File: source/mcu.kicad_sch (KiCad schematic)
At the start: 35 parts, among them J4 Conn_01x04_Male, J5 TYPE-C-31-M-12, U14 TJA1050T/CM,118, U15 STM32F405RGT6, Y1 8MHz Crystal Resonator, X5032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

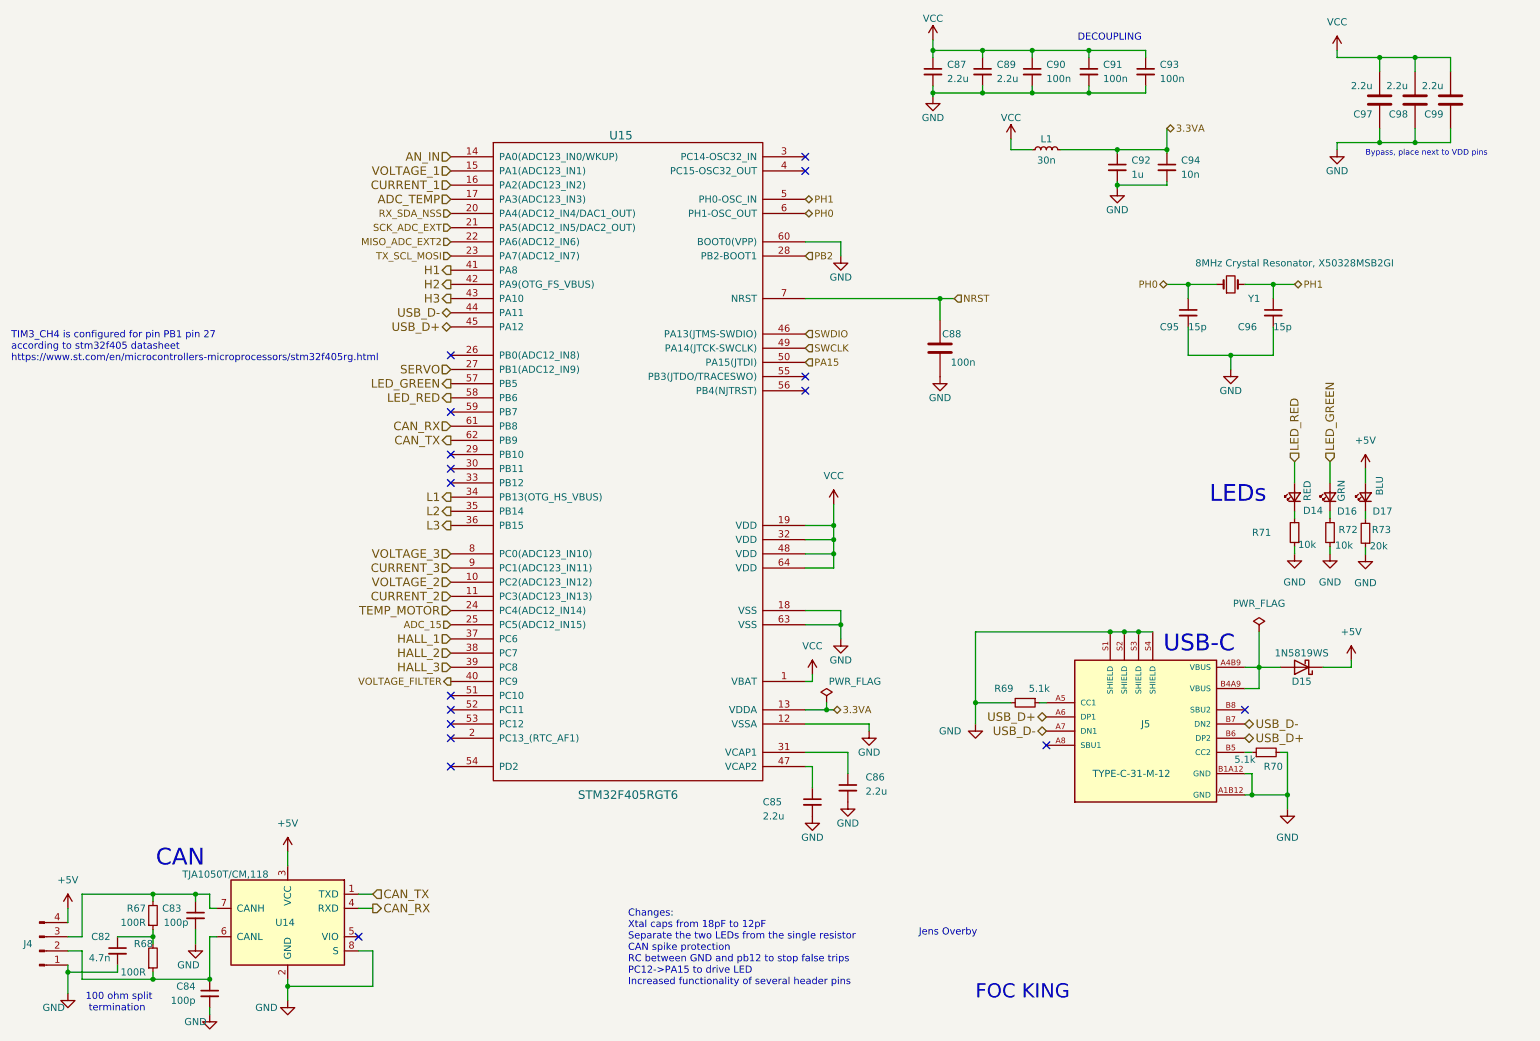
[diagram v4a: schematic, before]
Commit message: Add files via upload
Filter resistor on current op-amps changed from 30k to 150R
Mosfets at 45 deg angle
Changed layout of power supply
Cut through center of board
Unnecessary components near mosfets removed
Voltage filters removed again
Crystal suspected noise source - moved to back of board
Current sensing moved to in0 - in2 (PA0-PA2)
Voltage sensing moved to in11-in13
Supply voltage moved to in10
Mosfets can now be attached to heat-sink plate using screws (that can be tightened throug holes in the board)
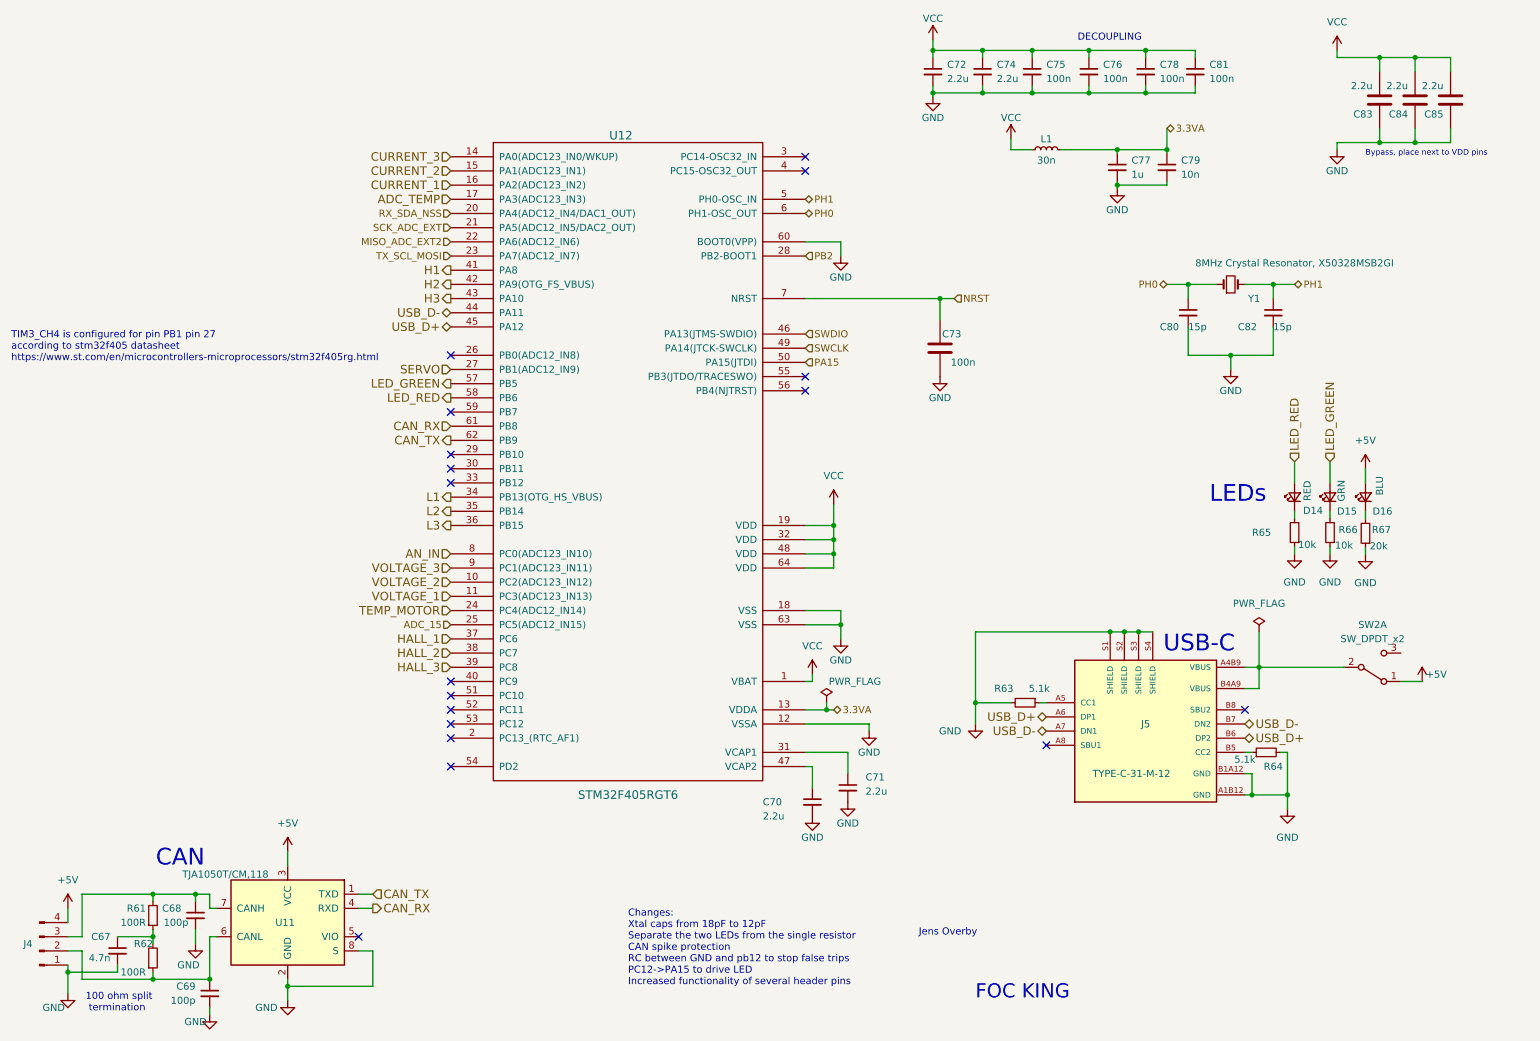
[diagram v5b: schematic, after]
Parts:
- removed D15: 1N5819WS, Diode_SMD:D_SOD-323, symbol Device:D_Schottky
- added C81: 100n, Capacitor_SMD:C_0603_1608Metric, symbol Device:C_Small
- added SW2: SW_DPDT_x2, Jumper:SolderJumper-2_P1.3mm_Open_Pad1.0x1.5mm, symbol Switch:SW_DPDT_x2
- renumbered C82 to C67, C83 to C68, C84 to C69, C85 to C70, C86 to C71, C87 to C72, C88 to C73, C89 to C74, C90 to C75, C91 to C76, C92 to C77, C93 to C78, C94 to C79, C95 to C80, C96 to C82, C97 to C83, C98 to C84, C99 to C85, D16 to D15, D17 to D16, R67 to R61, R68 to R62, R69 to R63, R70 to R64, R71 to R65, R72 to R66, R73 to R67, U14 to U11, U15 to U12
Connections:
- net +5V: now also SW2.1 (A)
- net AN_IN: now also U12.8 (PC0(ADC123_IN10)); no longer U12.14 (PA0(ADC123_IN0/WKUP))
- net CURRENT_2: now also U12.15 (PA1(ADC123_IN1)); no longer U12.11 (PC3(ADC123_IN13))
- net CURRENT_3: now also U12.14 (PA0(ADC123_IN0/WKUP)); no longer U12.9 (PC1(ADC123_IN11))
- net GND: now also C81.2
- net VCC: now also C81.1
- net VOLTAGE_1: now also U12.11 (PC3(ADC123_IN13)); no longer U12.15 (PA1(ADC123_IN1))
- net VOLTAGE_3: now also U12.9 (PC1(ADC123_IN11)); no longer U12.8 (PC0(ADC123_IN10))
- net at J5.A4B9 (VBUS), J5.B4A9 (VBUS): now also SW2.2 (B)
- net VOLTAGE_FILTER: no longer names the net of U12.40 (PC9)
- no-connect marks 17 -> 18

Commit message: 2 board setup with mcu and foc shield separated
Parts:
- removed C67: 4.7n, Capacitor_SMD:C_0603_1608Metric, symbol Device:C_Small
- removed C68, C69: 100p, Capacitor_SMD:C_0603_1608Metric, symbol Device:C_Small
- removed C72, C74: 2.2u, Capacitor_SMD:C_0603_1608Metric, symbol Device:C_Small
- removed C73: 100n, Capacitor_SMD:C_0603_1608Metric, symbol BLDC_4-rescue:C-RESCUE-BLDC_4
- removed C84, C85: 2.2u, Capacitor_SMD:C_0603_1608Metric, symbol BLDC_4-rescue:C-RESCUE-BLDC_4
- removed J4: Conn_01x04_Male, Connector_PinHeader_2.54mm:PinHeader_1x04_P2.54mm_Vertical, symbol Connector:Conn_01x04_Male
- removed R61, R62: 100R, Resistor_SMD:R_0603_1608Metric, symbol Device:R_Small
- removed U11: TJA1050T/CM,118, Package_SO:SOIC-8_3.9x4.9mm_P1.27mm, symbol Interface_CAN_LIN:TJA1051T-3
- added C67, C68: 100n, Capacitor_SMD:C_0603_1608Metric, symbol Device:C
- added C80: 10u, Capacitor_SMD:C_0603_1608Metric, symbol Device:C
- added JP1: SolderJumper_3_Open, Jumper:SolderJumper-3_P1.3mm_Open_RoundedPad1.0x1.5mm_NumberLabels, symbol Jumper:SolderJumper_3_Open
- added P1: SWD, Connector_PinHeader_2.54mm:PinHeader_1x05_P2.54mm_Vertical, symbol Connector_Generic:Conn_01x05
- added U11, U12: STM32F401CCU6_Blackpill, Custom:Blackpill_STM32F401CEU6, symbol CCC_ESC_Custom_Symbols:STM32F401CCU6_Balckpill
- C76: renamed from C80; value 15p -> 12p; LCSC C1644 -> C38523
- C78: renamed from C82; value 15p -> 12p; LCSC C1644 -> C38523
- C79: renamed from C83; value 2.2u -> 100n; LCSC C23630 -> C14663
- SW2: symbol Switch:SW_DPDT_x2 -> Switch:SW_DPST_x2
- renumbered C70 to C69, C71 to C70, C75 to C71, C76 to C72, C77 to C73, C78 to C74, C79 to C75, C81 to C77, R63 to R60, R64 to R61, R65 to R62, R66 to R63, R67 to R64, U12 to U13
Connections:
- net +5V: now also SW2.2 (B), U11.38 (5V), U12.21 (PB12), U12.38 (5V); no longer SW2.1 (A)
- net ADC_TEMP: now also C68.1, JP1.2 (C), JP1.3 (B), U11.15 (PB1), U12.15 (PB1)
- net AN_IN: now also U11.7 (PA1), U12.7 (PA1)
- net CAN_RX: now also U11.36 (PB8), U12.36 (PB8)
- net CAN_TX: now also U11.37 (PB9), U12.37 (PB9)
- net CURRENT_1: now also U11.8 (PA2), U12.8 (PA2)
- net CURRENT_2: now also U11.9 (PA3), U12.9 (PA3)
- net CURRENT_3: now also U11.10 (PA4), U12.10 (PA4)
- net GND: now also C67.2, C68.2, C80.2, P1.3 (Pin_3), U11.19 (GND), U11.39 (GND), U12.19 (GND), U12.39 (GND)
- net H1: now also U11.25 (PA8), U12.25 (PA8)
- net H2: now also U11.26 (PA9), U12.26 (PA9)
- net H3: now also U11.27 (PA10), U12.27 (PA10)
- net HALL_1: now also U11.2 (PC13), U12.2 (PC13)
- net HALL_2: now also U11.3 (PC14), U12.3 (PC14)
- net HALL_3: now also U11.4 (PC15), U12.4 (PC15)
- net L1: now also U11.22 (PB13), U12.22 (PB13)
- net L2: now also U11.23 (PB14), U12.23 (PB14)
- net L3: now also U11.24 (PB15), U12.24 (PB15)
- net NRST: now also C67.1, JP1.1 (A), P1.5 (Pin_5), U11.5 (NRST), U12.5 (NRST)
- net VCC: now also C80.1, P1.1 (Pin_1), U11.18 (3V3), U11.40 (3V3), U12.18 (3V3), U12.40 (3V3)
- net VOLTAGE_1: now also U11.11 (PA5), U12.11 (PA5)
- net VOLTAGE_2: now also U11.12 (PA6), U12.12 (PA6)
- net VOLTAGE_3: now also U11.14 (PB0), U12.14 (PB0)
- net CONN_12: now reaches U13.55 (PB3(JTDO/TRACESWO))
- net CONN_12: now also U11.6 (PA0), U12.6 (PA0)
- net at J5.A4B9 (VBUS), J5.B4A9 (VBUS): now also SW2.1 (A); no longer SW2.2 (B)
- net ADC_15 renamed CONN_5
- net CONN_5: now also U11.31 (PB3), U12.31 (PB3)
- net MISO_ADC_EXT2 renamed CONN_10
- net CONN_10: now also U11.17 (PB10), U12.17 (PB10)
- net PA15 renamed CONN_7
- net CONN_7: now also U11.33 (PB5), U12.33 (PB5)
- net PB2 renamed CONN_6
- net CONN_6: now also U11.32 (PB4), U12.32 (PB4)
- net RX_SDA_NSS renamed CONN_8
- net CONN_8: now also U11.34 (PB6), U12.34 (PB6)
- net SCK_ADC_EXT renamed CONN_9
- net CONN_9: now also U11.35 (PB7), U12.35 (PB7)
- net SERVO renamed SERVO_MOTORTEMP
- net SERVO_MOTORTEMP: now also U11.13 (PA7), U12.13 (PA7)
- net SWCLK: no longer names the net of U13.49 (PA14(JTCK-SWCLK))
- net SWCLK: now also P1.2 (Pin_2)
- net SWDIO: no longer names the net of U13.46 (PA13(JTMS-SWDIO))
- net SWDIO: now also P1.4 (Pin_4)
- net TEMP_MOTOR renamed CONN_4
- net CONN_4: now also U11.30 (PA15), U12.30 (PA15)
- net TX_SCL_MOSI renamed CONN_11
- net CONN_11: now also U11.16 (PB2), U12.16 (PB2)
- no-connect marks 18 -> 25
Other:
- note added: "Black pill"
- note added: "Bluepill / GD32F303 / Artery AT403pill"
- note added: "Brake or motor temp inputs"
- note added: "Input impedance 470R on every (CONN) pin makes it much more resilient to ESD, cross wiring, GPIO-GND/3V3 etc"
- note added: "Likely use case: PWM Throttle Encoder on SPI, SSI or Incremental Peripherals GPIO"
- note added: "Likely use case: PWM Throttle Incremental Encoder Screen Comms Peripherals GPIO"
- note added: "MISO and MOSI are useful to have a link in case of one wire SSI DNP if full duplex required (Connect PB4, PB5 with 2k2 resistor)"
- note added: "Not connected for blue/black pill compatibility reasons"
- note added: "Phase sensing"
- note added: "Reserved PWM"
- note added: "Reserved for USB DO NOT CONNECT"
- note added: "THROTTLE"
- note removed: "100 ohm split termination"
- note removed: "CAN"

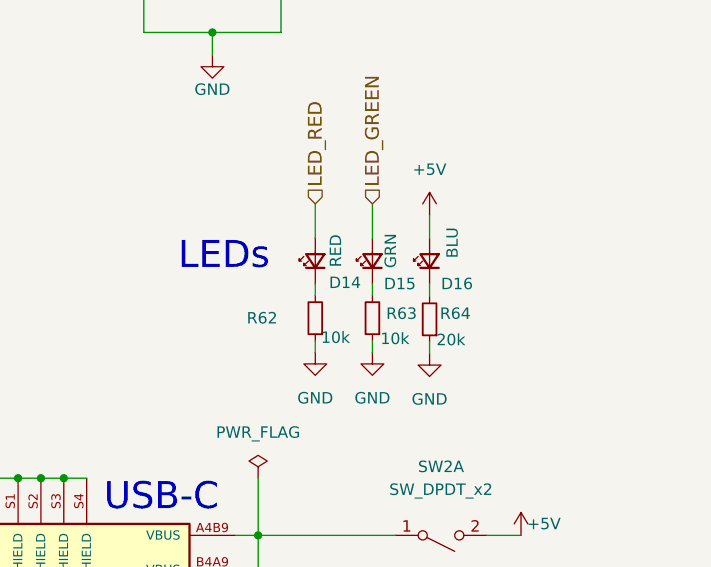
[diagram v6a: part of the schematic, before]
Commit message: Add files via upload
2 missing gnd connections on mcu
missing gnd connection on 12V power supply
pin4 pulled to gnd on 5V power supply
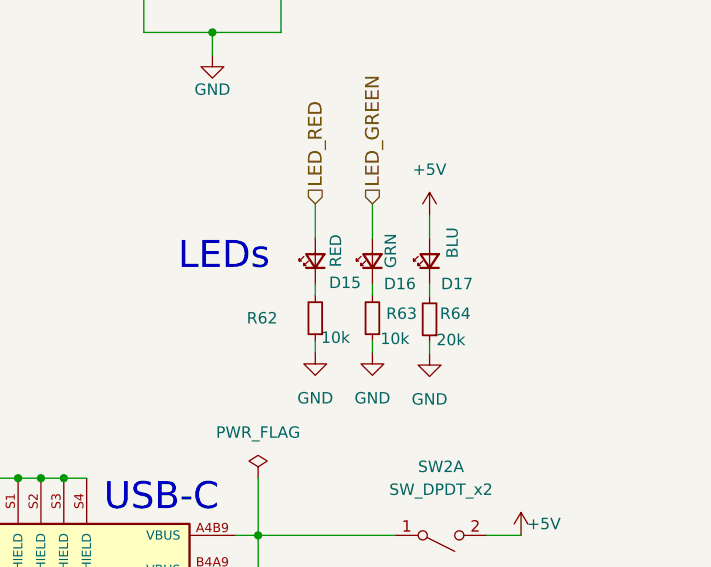
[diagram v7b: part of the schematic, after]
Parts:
- renumbered D14 to D15, D15 to D16, D16 to D17
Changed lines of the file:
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@@
   (symbol (lib_id "Device:LED_Small") (at 245.11 101.6 90) (unit 1)
     (in_bom yes) (on_board yes)
-    (property "Reference" "D14" (id 0) (at 246.634 104.013 90)
+    (property "Reference" "D15" (id 0) (at 246.634 104.013 90)
       (effects (font (size 1.27 1.27)) (justify right))
     )
@@
   (symbol (lib_id "Device:LED_Small") (at 251.46 101.6 90) (unit 1)
     (in_bom yes) (on_board yes)
-    (property "Reference" "D15" (id 0) (at 252.73 104.14 90)
+    (property "Reference" "D16" (id 0) (at 252.73 104.14 90)
       (effects (font (size 1.27 1.27)) (justify right))
     )
@@
   (symbol (lib_id "Device:LED_Small") (at 257.81 101.6 90) (unit 1)
     (in_bom yes) (on_board yes)
-    (property "Reference" "D16" (id 0) (at 259.08 104.14 90)
-      (effects (font (size 1.27 1.27)) (justify right))
-    )
+    (property "Reference" "D17" (id 0) (at 259.08 104.14 90)
+      (effects (font (size 1.27 1.27)) (justify right))
+    )

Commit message: JLCPCB order with separate power supply
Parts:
- renumbered C67 to C61, C68 to C62, C69 to C63, C70 to C64, C71 to C65, C72 to C66, C73 to C67, C74 to C68, C75 to C69, C76 to C70, C77 to C71, C78 to C72, C79 to C73, C80 to C74, J5 to J4, P1 to P13
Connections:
- net H1: now also U11.24 (PB15), U12.24 (PB15); no longer U11.25 (PA8), U12.25 (PA8)
- net H2: now also U11.23 (PB14), U12.23 (PB14); no longer U11.26 (PA9), U12.26 (PA9)
- net H3: now also U11.22 (PB13), U12.22 (PB13); no longer U11.27 (PA10), U12.27 (PA10)
- net L1: now also U11.27 (PA10), U12.27 (PA10); no longer U11.22 (PB13), U12.22 (PB13)
- net L2: now also U11.26 (PA9), U12.26 (PA9); no longer U11.23 (PB14), U12.23 (PB14)
- net L3: now also U11.25 (PA8), U12.25 (PA8); no longer U11.24 (PB15), U12.24 (PB15)
- removed net CONN_10: U11.17 (PB10), U12.17 (PB10), U13.22 (PA6(ADC12_IN6))
- removed net CONN_11: U11.16 (PB2), U12.16 (PB2), U13.23 (PA7(ADC12_IN7))
- removed net CONN_12: U11.6 (PA0), U12.6 (PA0), U13.55 (PB3(JTDO/TRACESWO))
- removed net CONN_4: U11.30 (PA15), U12.30 (PA15), U13.24 (PC4(ADC12_IN14))
- removed net CONN_5: U11.31 (PB3), U12.31 (PB3), U13.25 (PC5(ADC12_IN15))
- removed net CONN_6: U11.32 (PB4), U12.32 (PB4), U13.28 (PB2-BOOT1)
- removed net CONN_7: U11.33 (PB5), U12.33 (PB5), U13.50 (PA15(JTDI))
- removed net CONN_8: U11.34 (PB6), U12.34 (PB6), U13.20 (PA4(ADC12_IN4/DAC1_OUT))
- removed net CONN_9: U11.35 (PB7), U12.35 (PB7), U13.21 (PA5(ADC12_IN5/DAC2_OUT))
- no-connect marks 25 -> 52
